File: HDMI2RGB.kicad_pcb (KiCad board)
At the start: 4 copper layers, 58.4 x 63.5 mm, 96 parts, among them J1 HDMI_A, J2 QTH-030-02-L-DA, P1 CONN_02X07, U1 TPD4S010DQAR, U2 TPD4S010DQAR, U5 ADV7611

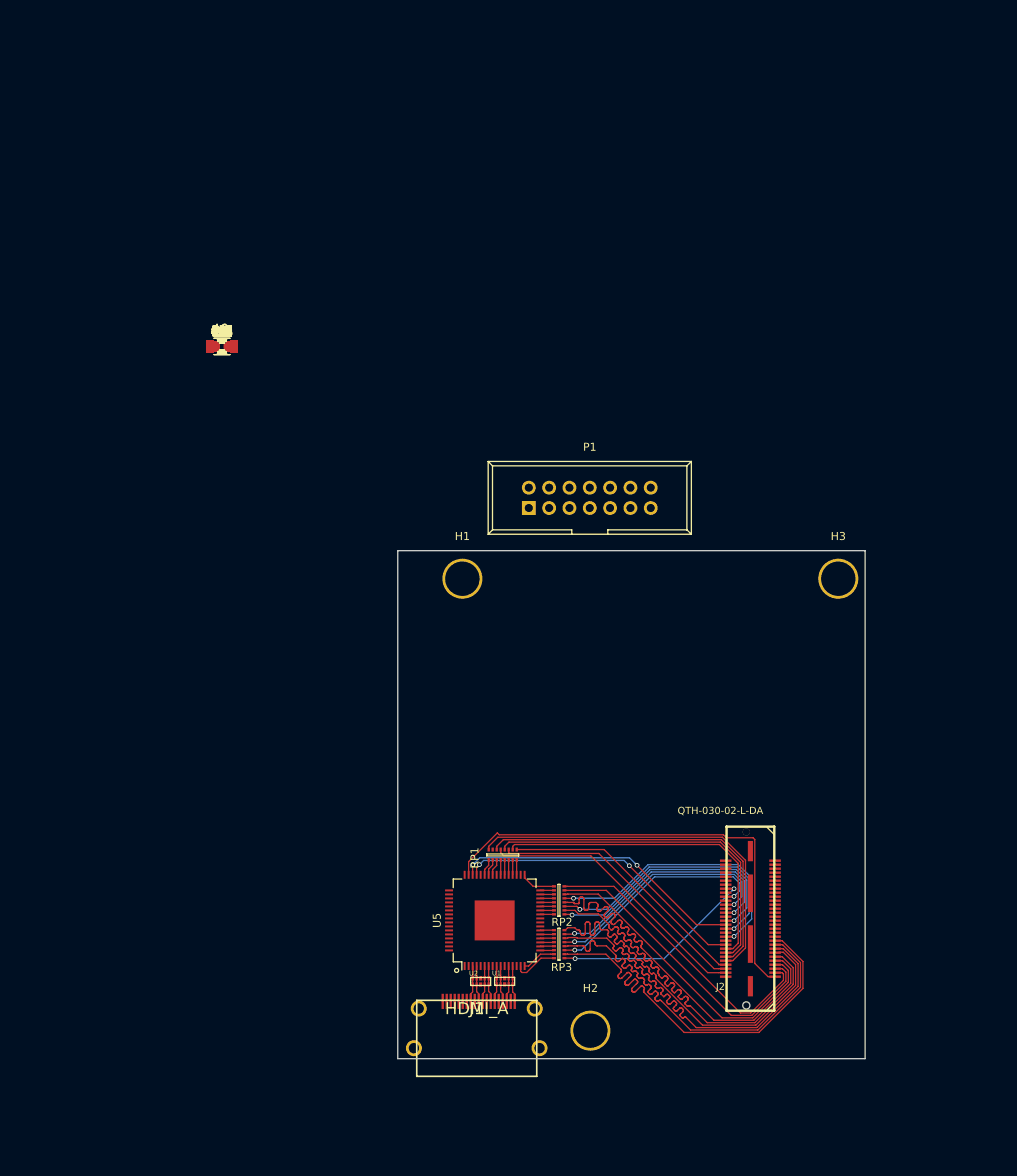
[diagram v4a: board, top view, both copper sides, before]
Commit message: ADV7611 power caps are placed and routed
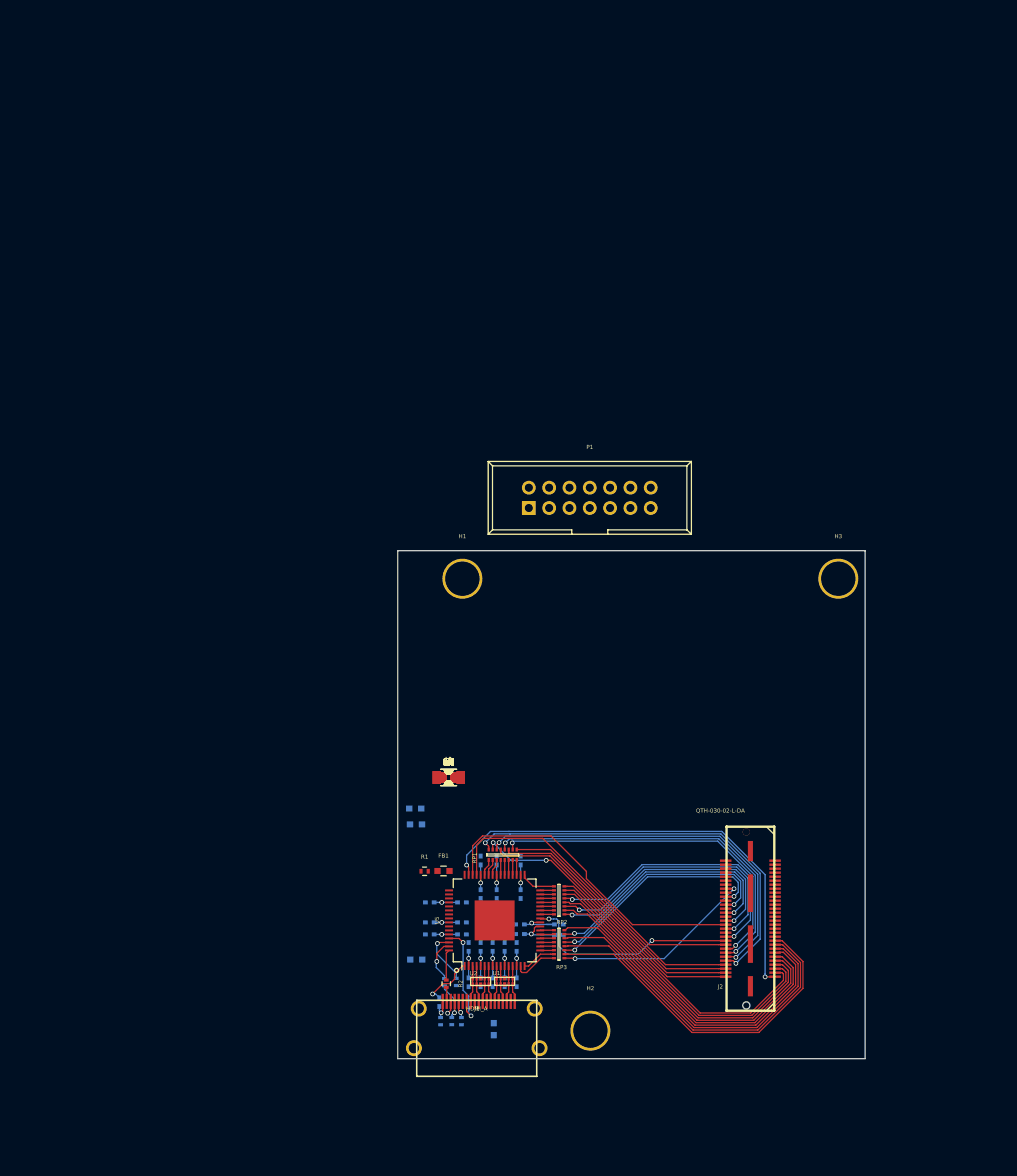
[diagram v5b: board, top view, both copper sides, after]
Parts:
- C1, C10, C11, C12, C15, C16, C17, C18, C19, C2, C20, C21, C22, C23, C24, C25, C26, C27, C28, C3, C4, C5, C6, C7, C8, C9, FB2, FB3, FB4, FB5, R10, R3, R4, R5, R8, R9: moved to B.Cu
- moved FB2 91.9 mm to (57.7, 123.3), turned to 90 degrees
- moved R3 89.5 mm to (53.7, 122.3), turned to 90 degrees
- moved R4 89.1 mm to (52.5, 122.3), turned to 90 degrees
- moved R5 88.7 mm to (51.1, 122.3), turned to 90 degrees
- moved C18 87.6 mm to (60.6, 117.5), turned to 270 degrees
- moved C6 87.0 mm to (59.1, 117.5), turned to 270 degrees
- moved C4 86.4 mm to (57.6, 117.5), turned to 270 degrees
- moved R10 86.3 mm to (50.9, 119.9), turned to 90 degrees
- moved C2 85.8 mm to (56.1, 117.5), turned to 270 degrees
- moved C15 85.2 mm to (54.6, 117.5), turned to 270 degrees
- moved C11 84.8 mm to (65.9, 111.5)
- moved R9 84.7 mm to (53.0, 117.4), turned to 270 degrees
- moved R2 84.4 mm to (51.8, 117.6), turned to 270 degrees
- moved R8 84.2 mm to (51.6, 117.4), turned to 270 degrees
- moved C24 83.6 mm to (65.9, 110.2)
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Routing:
- net /CONNECTOR/PDATA1: track 0.00 -> 36.9 mm, vias 0 -> 2
- net PCLK: track 0.00 -> 27.6 mm, vias 0 -> 2
- net /HDMI_INPUT/ADV_DVDD: track 0.00 -> 16.2 mm, vias 0 -> 4
- net /HDMI_INPUT/ADV_DVDDIO: track 0.00 -> 14.0 mm, vias 0 -> 3
- net /HDMI_INPUT/HDMI_CEC: track 0.00 -> 13.6 mm, vias 0 -> 2
- net /HDMI_INPUT/ADV_TVDD: track 0.00 -> 13.0 mm, vias 0 -> 3
- net /CONNECTOR/PDATA12: track 50.6 -> 40.5 mm
- net /CONNECTOR/PDATA14: track 50.8 -> 41.3 mm
- net /CONNECTOR/PDATA16: track 50.8 -> 41.5 mm
- net /HDMI_INPUT/ADV_CVDD: track 0.00 -> 8.74 mm, vias 0 -> 2
- net /CONNECTOR/PDATA18: track 50.9 -> 42.5 mm
- net /CONNECTOR/PDATA20: track 50.9 -> 43.3 mm
- net Net-(R9-Pad1): track 0.00 -> 6.90 mm, vias 0 -> 1
- net Net-(R10-Pad2): track 0.00 -> 6.87 mm, vias 0 -> 1
- net /CONNECTOR/PDATA22: track 50.8 -> 44.1 mm
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
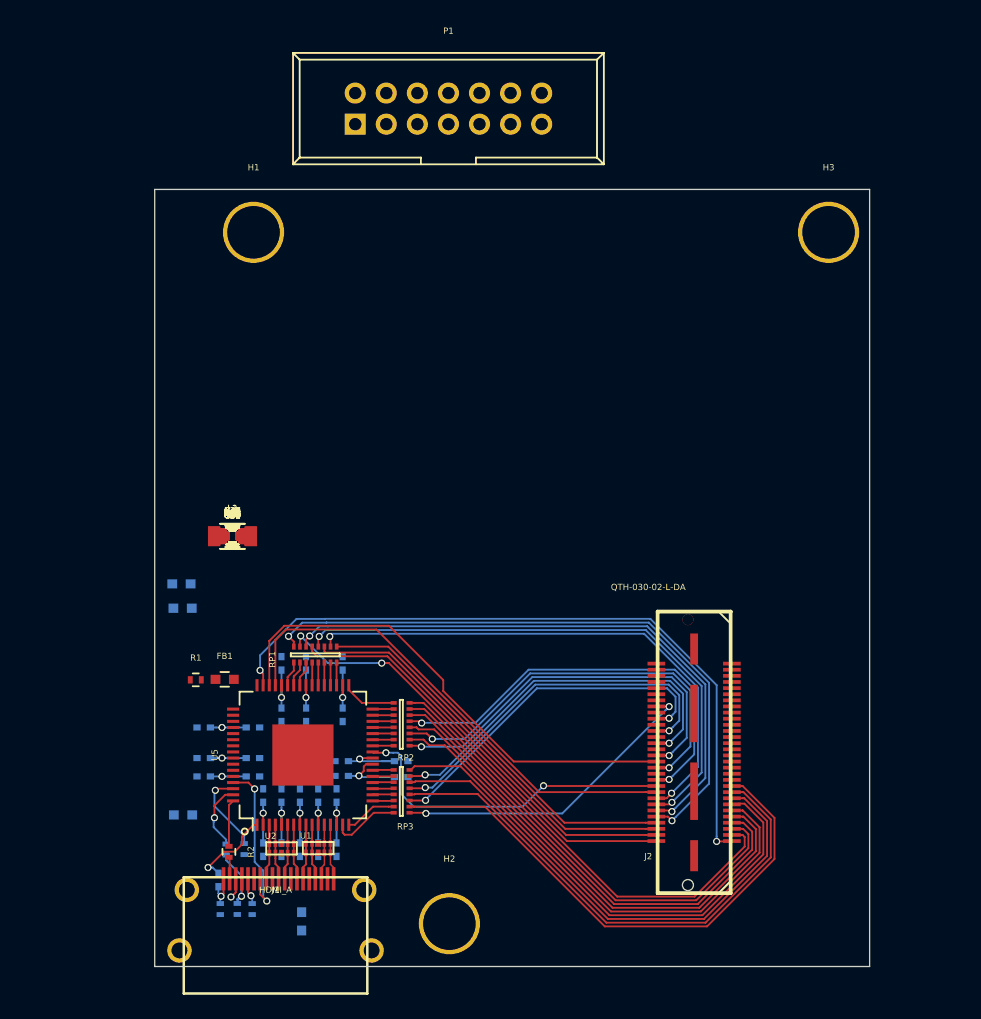
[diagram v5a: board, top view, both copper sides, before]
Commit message: Basic layout of all components on PCB
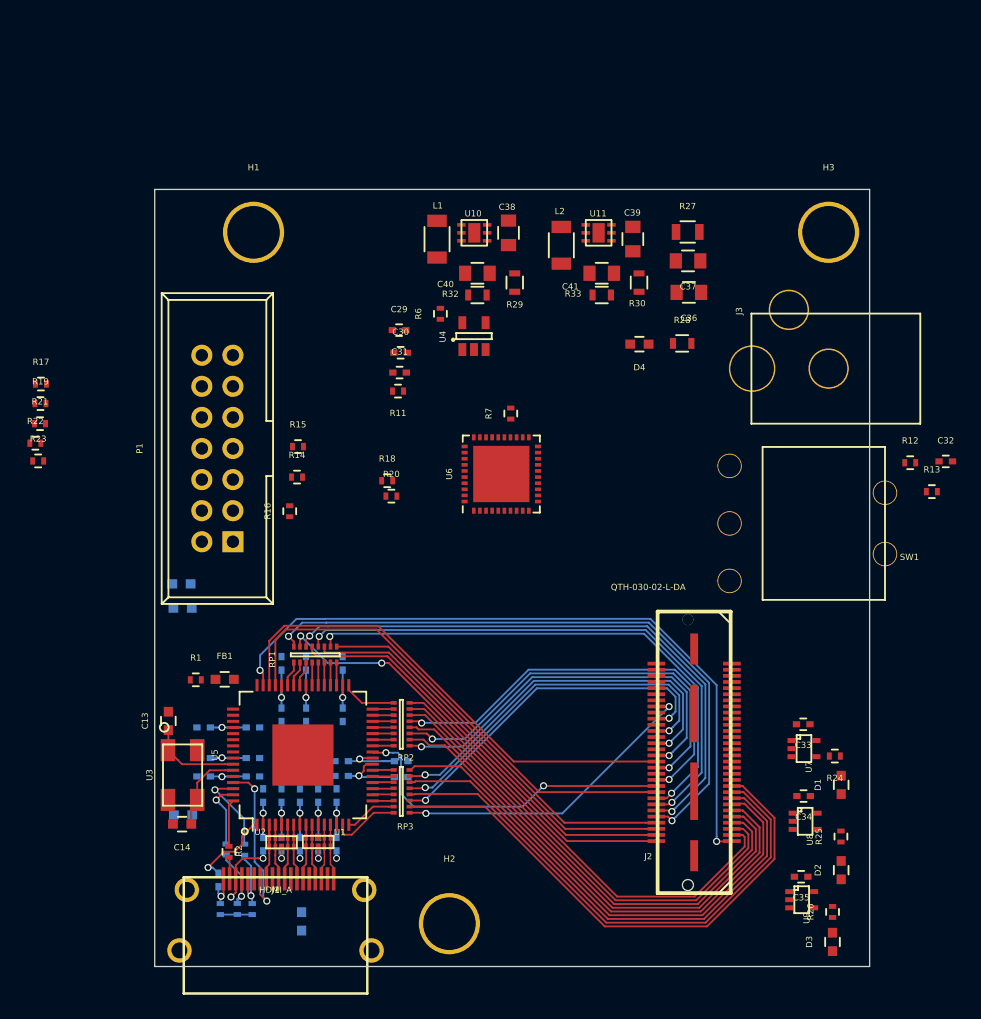
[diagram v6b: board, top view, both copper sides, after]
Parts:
- added J3: RAPC712x, misc:RAPC712, F.Cu at (108.3, 78.1)
- added SW1: 2M1-SP1-T2-B4-M6RE, misc:2M1-SP1-T2-B4-M6RE, F.Cu at (105.4, 90.8)
- added U10: TPS62260, misc:WSON-6, F.Cu at (71.8, 67.0)
- added U11: TPS62260, misc:WSON-6, F.Cu at (82.0, 67.0)
- added U3: ABM3B-24.000MHZ-B2-T, SMD_Packages:XTAL_ABRACON, F.Cu at (48.0, 111.4)
- added U4: TPS2061, TO_SOT_Packages_SMD:SOT-23-5, F.Cu at (71.8, 75.5)
- added U6: MSP430F2274TRHAR, Housings_DFN_QFN:QFN-40-1EP_6x6mm_Pitch0.5mm, F.Cu at (74.0, 86.8)
- added U7: SN74AUP1G06DCKR, TO_SOT_Packages_SMD:SC-70-5, F.Cu at (98.8, 109.2)
- added U8: SN74AUP1G07DCKR, TO_SOT_Packages_SMD:SC-70-5, F.Cu at (98.9, 115.1)
- added U9: SN74AUP1G06DCKR, TO_SOT_Packages_SMD:SC-70-5, F.Cu at (98.6, 121.5)
- moved D3 59.2 mm to (101.1, 125.0), turned to 90 degrees
- moved C32 58.6 mm to (110.4, 85.7)
- moved R26 57.9 mm to (101.1, 122.5), turned to 90 degrees
- moved R13 57.3 mm to (109.2, 88.2)
- moved D2 56.7 mm to (101.8, 119.1), turned to 90 degrees
- moved R12 55.7 mm to (107.5, 85.8)
- moved R25 55.4 mm to (101.8, 116.4), turned to 90 degrees
- moved C35 54.2 mm to (98.5, 119.7), turned to 180 degrees
- moved D1 53.7 mm to (101.8, 112.2), turned to 90 degrees
- moved R24 52.4 mm to (101.3, 109.8), turned to 180 degrees
- moved C34 51.3 mm to (98.7, 113.1), turned to 180 degrees
- moved C33 49.1 mm to (98.7, 107.2), turned to 180 degrees
- moved R27 44.8 mm to (89.3, 67.0)
- moved C37 43.5 mm to (89.3, 69.3), turned to 180 degrees
- moved C36 42.3 mm to (89.4, 71.9), turned to 180 degrees
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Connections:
- C32 pad 2: Net-(C32-Pad2) -> GND
- R12 pad 1: Net-(R12-Pad1) -> /MSP430/MSP_VDD3V3
- R13 pad 2: Net-(R13-Pad2) -> GND
- R27 pad 2: GND -> Net-(J3-Pad2)
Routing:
- net GND: track 1.65 -> 10.3 mm, vias 1 -> 6
- net Net-(C13-Pad1): track 0.00 -> 7.46 mm
- net Net-(C14-Pad1): track 0.00 -> 6.94 mm
- net /HDMI_INPUT/HDMI_SCL: track 2.16 -> 5.69 mm
- net +3V3: track 0.00 -> 2.61 mm
- net /HDMI_INPUT/ADV_TVDD: track 13.0 -> 11.7 mm
- net /HDMI_INPUT/ADV_CVDD: track 8.74 -> 7.85 mm
- net HSYNC_CS: track 40.9 -> 40.4 mm
- added copper zone on In1.Cu, net GND
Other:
- net class Default: via_dia 0.5842 -> 0.5588
- net class POWER_IN added: clearance 0.1524, trace_width 508, via_dia 0.5588, via_drill 0.381
- rule via_min_size: 0.5842 -> 0.5588

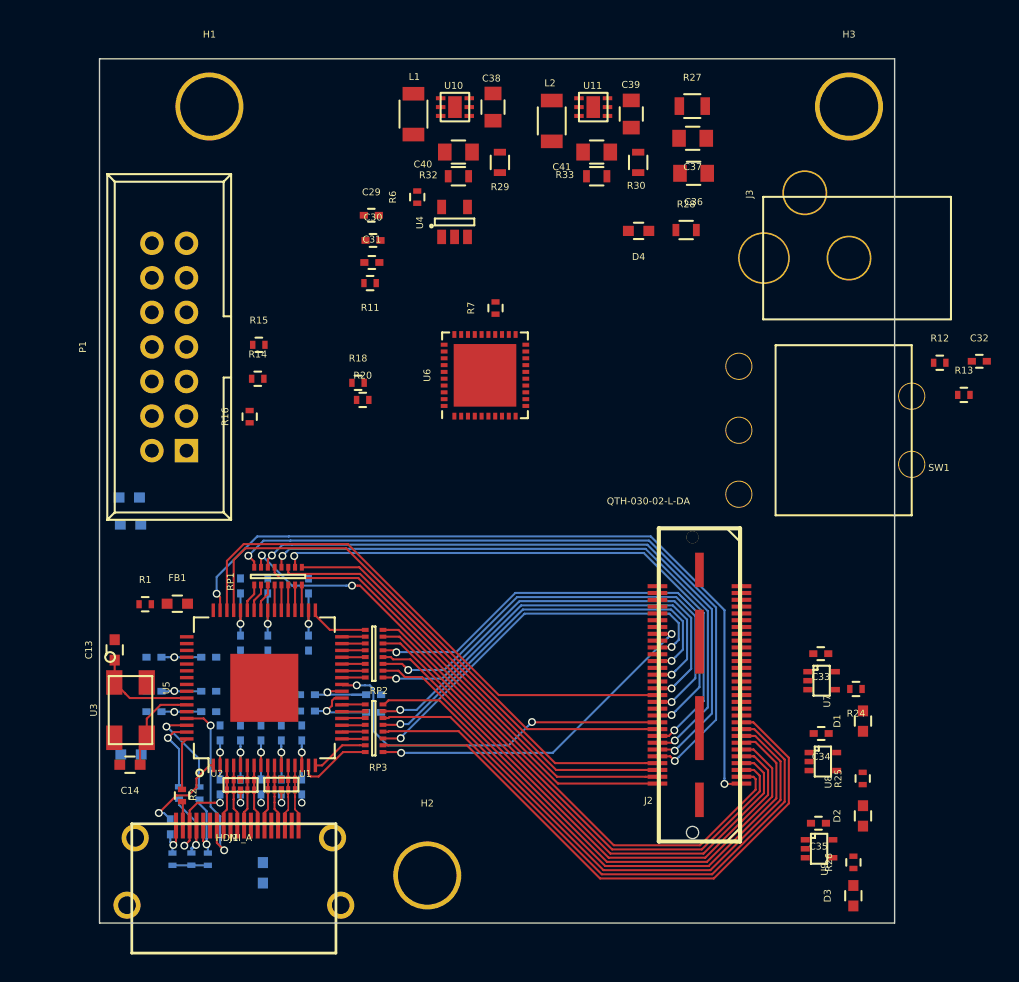
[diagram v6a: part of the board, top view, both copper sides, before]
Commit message: Routing power, changed buttons connections, and a few pther connections
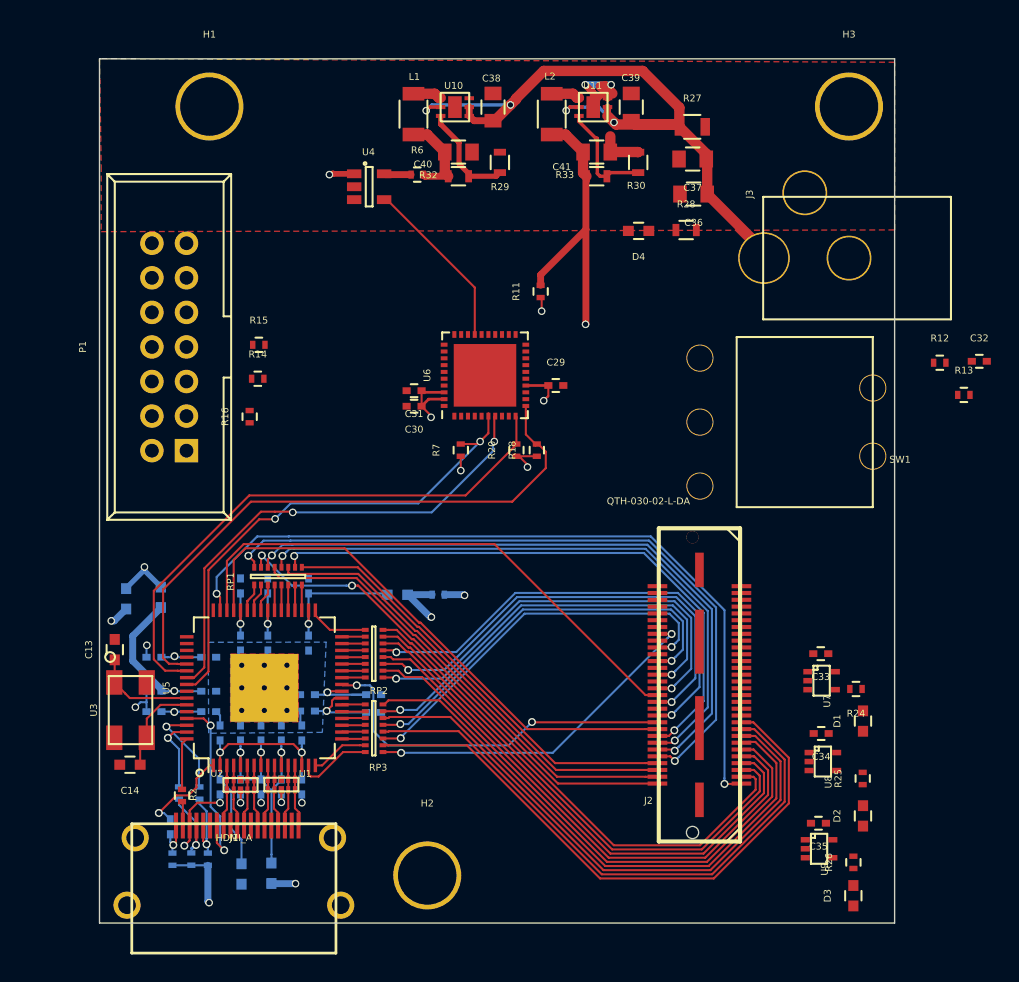
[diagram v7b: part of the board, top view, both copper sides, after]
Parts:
- FB1, R1: moved to B.Cu
- U5: footprint ADV7611:LQFP-64_TH_10x10mm_Pitch0.5mm -> misc:LQFP-64_TH_10x10mm_Pitch0.5mm
- moved R1 21.5 mm to (70.6, 102.9)
- moved C29 18.4 mm to (79.2, 87.5)
- moved FB1 16.2 mm to (67.6, 102.9), turned to 180 degrees
- moved R18 14.0 mm to (77.9, 92.3), turned to 90 degrees
- moved C30 12.6 mm to (68.8, 89.0), turned to 180 degrees
- moved R11 12.5 mm to (78.1, 80.6), turned to 90 degrees
- moved FB3 12.0 mm to (56.2, 123.4), turned to 90 degrees
- moved R20 11.9 mm to (76.4, 92.3), turned to 90 degrees
- moved R7 10.7 mm to (72.3, 92.3)
- moved C31 9.92 mm to (68.8, 87.9), turned to 180 degrees
- moved FB5 7.69 mm to (50.2, 103.1), turned to 270 degrees
- moved U4 6.79 mm to (65.5, 72.9), turned to 0 degrees
- moved FB4 5.46 mm to (47.7, 103.2), turned to 270 degrees
- moved SW1 2.92 mm to (102.5, 90.2)
- moved R6 1.65 mm to (69.1, 72.0), turned to 0 degrees
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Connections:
- R18 pad 1: +3V3 -> /MSP430/MSP_VDD3V3
- R20 pad 1: +3V3 -> /MSP430/MSP_VDD3V3
- U6 pad 15: Net-(U6-Pad15) -> /MSP430/PB_UP
- U6 pad 16: Net-(U6-Pad16) -> /MSP430/PB_DOWN
- U6 pad 17: Net-(U6-Pad17) -> /MSP430/PB_LEFT
- U6 pad 18: Net-(U6-Pad18) -> /MSP430/PB_RIGHT
- U6 pad 19: Net-(U6-Pad19) -> /MSP430/PB_SELECT
- U6 pad 24: RESET_ADV7611 -> Net-(U6-Pad24)
- U6 pad 25: HDMI_INT1 -> Net-(U6-Pad25)
- U6 pad 26: ADV_1V8_EN -> Net-(U6-Pad26)
- U6 pad 27: /MSP430/PB_RIGHT -> ADV_1V8_EN
- U6 pad 28: /MSP430/PB_SELECT -> Net-(U6-Pad28)
- U6 pad 6: /MSP430/PB_UP -> RESET_ADV7611
- U6 pad 7: /MSP430/PB_DOWN -> HDMI_INT1
- U6 pad 8: /MSP430/PB_LEFT -> Net-(U6-Pad8)
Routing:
- net +3V3: track 2.61 -> 97.9 mm, vias 0 -> 4
- net SYSPWR: track 0.00 -> 58.3 mm, vias 0 -> 4
- net MSP_I2C_SCL: track 0.00 -> 44.2 mm
- net /HDMI_INPUT/ADV_VDD1V8: track 0.00 -> 42.0 mm, vias 0 -> 2
- net MSP_I2C_SDA: track 0.00 -> 41.0 mm
- net /MSP430/MSP_VDD3V3: track 0.00 -> 39.9 mm, vias 0 -> 4
- net RESET_ADV7611: track 0.00 -> 37.2 mm, vias 0 -> 2
- net HDMI_INT1: track 0.00 -> 36.5 mm, vias 0 -> 2
- net /HDMI_INPUT/ADV_VDD3V3: track 0.00 -> 31.0 mm, vias 0 -> 2
- net GND: track 10.3 -> 27.2 mm, vias 6 -> 10
- net /HDMI_INPUT/ADV_CVDD: track 7.85 -> 21.2 mm
- net ADV_1V8_EN: track 0.00 -> 12.8 mm
- net /HDMI_INPUT/ADV_TVDD: track 11.7 -> 20.9 mm
- net Net-(R30-Pad1): track 0.00 -> 8.05 mm
- net /HDMI_INPUT/ADV_PVDD: track 3.05 -> 10.9 mm
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- added copper zone on B.Cu, net GND
- added copper zone on F.Cu, net GND
